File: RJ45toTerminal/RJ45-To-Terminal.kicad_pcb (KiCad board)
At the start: 2 copper layers, 69.5 x 58.1 mm, 70 parts, among them J11 Screw_Terminal_01x08, J12 Screw_Terminal_01x08, J13 Screw_Terminal_01x08, J14 Screw_Terminal_01x08

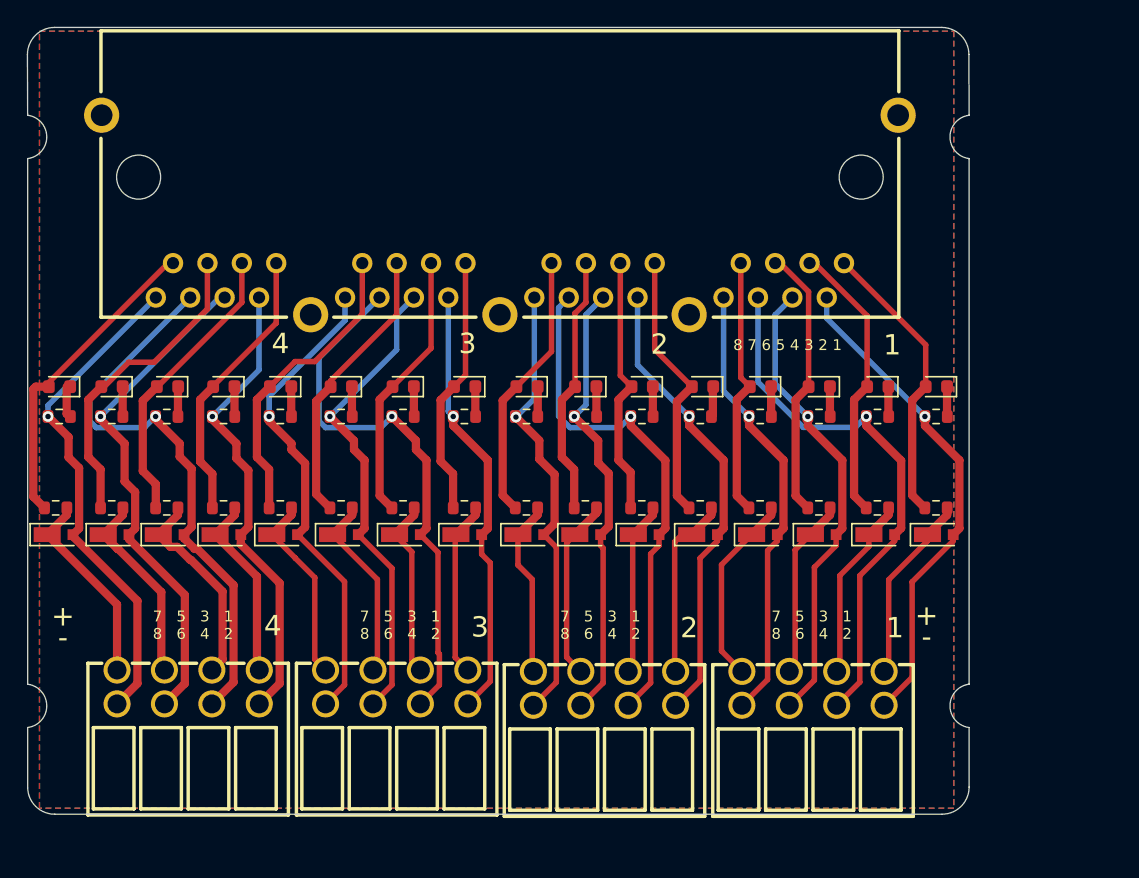
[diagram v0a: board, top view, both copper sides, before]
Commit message: updated RJ45ToTerminal with additional space between pluggable conenctor
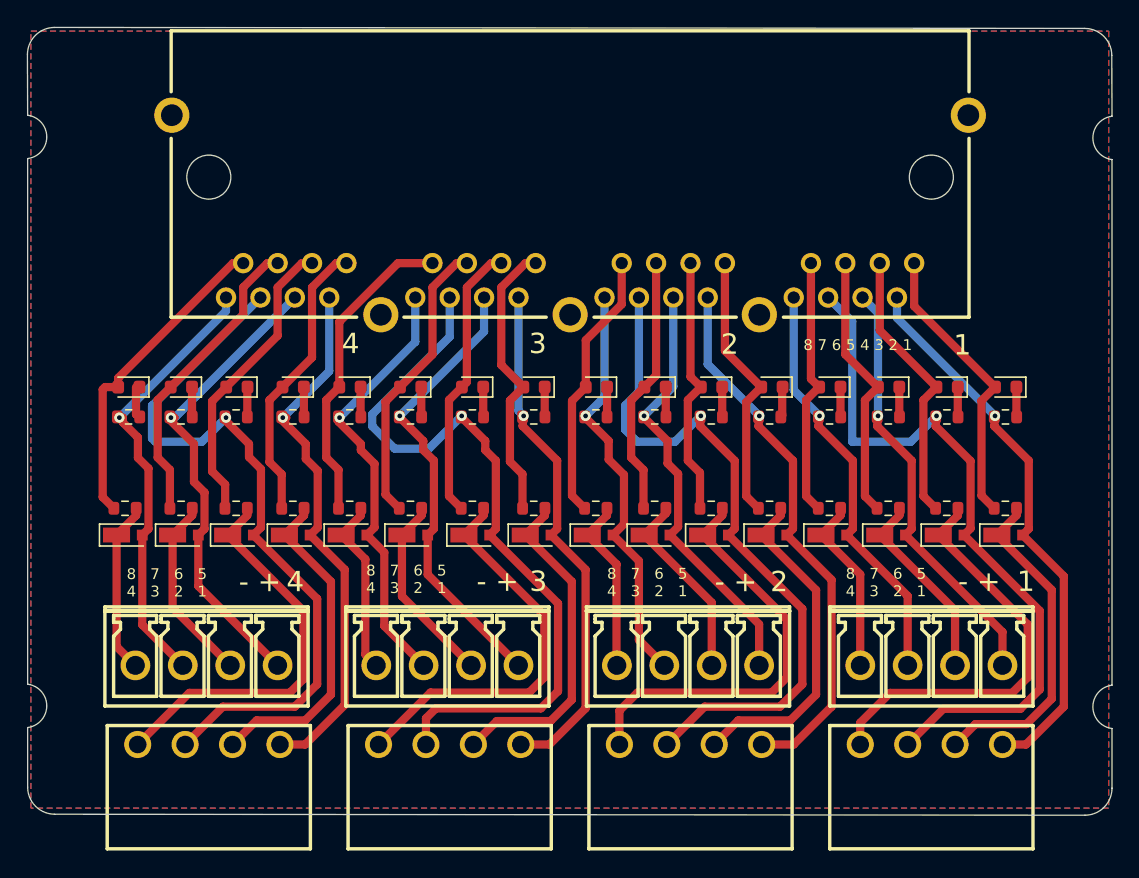
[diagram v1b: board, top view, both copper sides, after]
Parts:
- added J16: Screw_Terminal_01x04, Footprints:CONN-TH_XY2500V-F-3.5-4P, F.Cu at (163.6, 109.1)
- added J17: Screw_Terminal_01x04, Footprints:CONN-TH_XY2500R-G-3.5-4P, F.Cu at (163.8, 114.9)
- added J18: Screw_Terminal_01x04, Footprints:CONN-TH_XY2500V-F-3.5-4P, F.Cu at (181.6, 109.1)
- added J19: Screw_Terminal_01x04, Footprints:CONN-TH_XY2500R-G-3.5-4P, F.Cu at (181.6, 114.9)
- J11, J13: value Screw_Terminal_01x08 -> Screw_Terminal_01x04; footprint VizistaHA:CONN-TH_4P-P3.50_JILN_JL15EDGRHC-35004B02 -> Footprints:CONN-TH_XY2500V-F-3.5-4P
- J12, J14: value Screw_Terminal_01x08 -> Screw_Terminal_01x04; footprint VizistaHA:CONN-TH_4P-P3.50_JILN_JL15EDGRHC-35004B02 -> Footprints:CONN-TH_XY2500R-G-3.5-4P
- moved J14 27.1 mm to (146.1, 114.9)
- moved J12 14.5 mm to (128.3, 114.9)
- moved J13 11.7 mm to (145.9, 109.1)
- moved G*** 5.18 mm to (155.6, 71.1)
- moved RJ45-1 5.18 mm to (154.9, 75.8)
- moved D54 5.12 mm to (134.7, 99.5)
- moved D55 5.12 mm to (138.9, 99.5)
- moved D58 5.12 mm to (152.5, 99.5)
- moved D59 5.12 mm to (157.1, 99.5)
- moved D61 5.12 mm to (165.6, 99.5)
- moved D64 5.12 mm to (178.7, 99.5)
- moved LED59 5.12 mm to (156.9, 88.5)
- moved LED62 5.12 mm to (169.8, 88.5)
- moved LED64 5.12 mm to (178.5, 88.5)
- moved R54 5.12 mm to (134.5, 90.8)
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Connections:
- J12 pad 1: RC12- -> RC14-
- J12 pad 2: IN12- -> IN14-
- J12 pad 3: RC11- -> RC13-
- J12 pad 4: IN11- -> IN13-
- J13 pad 1: RC8- -> RC12-
- J13 pad 2: IN8- -> IN12-
- J13 pad 3: RC7- -> RC11-
- J13 pad 4: IN7- -> IN11-
- J14 pad 1: RC4- -> RC10-
- J14 pad 2: IN4- -> IN10-
- J14 pad 3: RC3- -> RC9-
- J14 pad 4: IN3- -> IN9-
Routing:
- net RC6-: track 12.8 -> 31.5 mm
- net RC2-: track 13.7 -> 31.2 mm
- net RC10-: track 13.4 -> 29.8 mm
- net IN10-: track 40.5 -> 56.5 mm
- net RC14-: track 15.2 -> 29.8 mm
- net IN6-: track 38.6 -> 52.2 mm
- net IN2-: track 40.3 -> 53.7 mm
- net IN14-: track 42.4 -> 54.7 mm
- net RC9-: track 13.0 -> 24.8 mm
- net RC5-: track 13.6 -> 25.1 mm
- net RC1-: track 14.0 -> 24.9 mm
- net RC13-: track 13.9 -> 24.6 mm
- net IN5-: track 34.2 -> 40.8 mm
- net IN9-: track 32.3 -> 38.8 mm
- net IN13-: track 34.6 -> 40.4 mm
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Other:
- board size 69.5 x 58.1 mm -> 80.1 x 58.2 mm
- board text removed: "7 5 3 1 8 6 4 2"
- board text removed: "Based on design by Jon Oxer by Austin's Creations"

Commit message: fixes
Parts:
- added H1: MountingHole, MountingHole:MountingHole_3.2mm_M3, F.Cu at (118.8, 70.0)
- added H2: MountingHole, MountingHole:MountingHole_3.2mm_M3, F.Cu at (191.0, 70.0)
- added H3: MountingHole, MountingHole:MountingHole_3.2mm_M3, F.Cu at (116.5, 116.4)
- added H4: MountingHole, MountingHole:MountingHole_3.2mm_M3, F.Cu at (192.9, 116.4)
- added H5: MountingHole, MountingHole:MountingHole_3.2mm_M3, F.Cu at (118.8, 83.1)
- added H6: MountingHole, MountingHole:MountingHole_3.2mm_M3, F.Cu at (191.0, 83.1)
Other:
- outline, holes or cut-outs redrawn
